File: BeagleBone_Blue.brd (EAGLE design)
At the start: 385 parts, among them J1 HEADER_6, P1 PJ-200A, P10 MOLEX_502570-001, P2 CTI_JTAG,DNI, P3 USB-A_Conn._-_87520-xx1xx, P4 mini_USB-B, P5 WE_7499010211A, P6 10118241-001RLF, P8 FEMALE_HEADER_2x23, P9 FEMALE_HEADER_2x23, Q1 DMC56404, Q2 DMC56404, U10 TPD4S012, U11 TDA19988, U12 MT41K256M16HA_-125:E, U13 eMMC,_2GB, U14 LAN8710A, U15 SN74LVC2G241, U2 TPS65217C, U3 SN74LVC1G06DCK, U4 TL5209, U5 IC_AM335X_ZCE_1, U6 SN74LVC1G74DCTR, U7 24LC32A, U8 TPS2051__DGN_, U9 TPD4S012, Y1 32.768kHz, Y2 24MHz, Y3 25.000MHz, Y4 24.576MHz

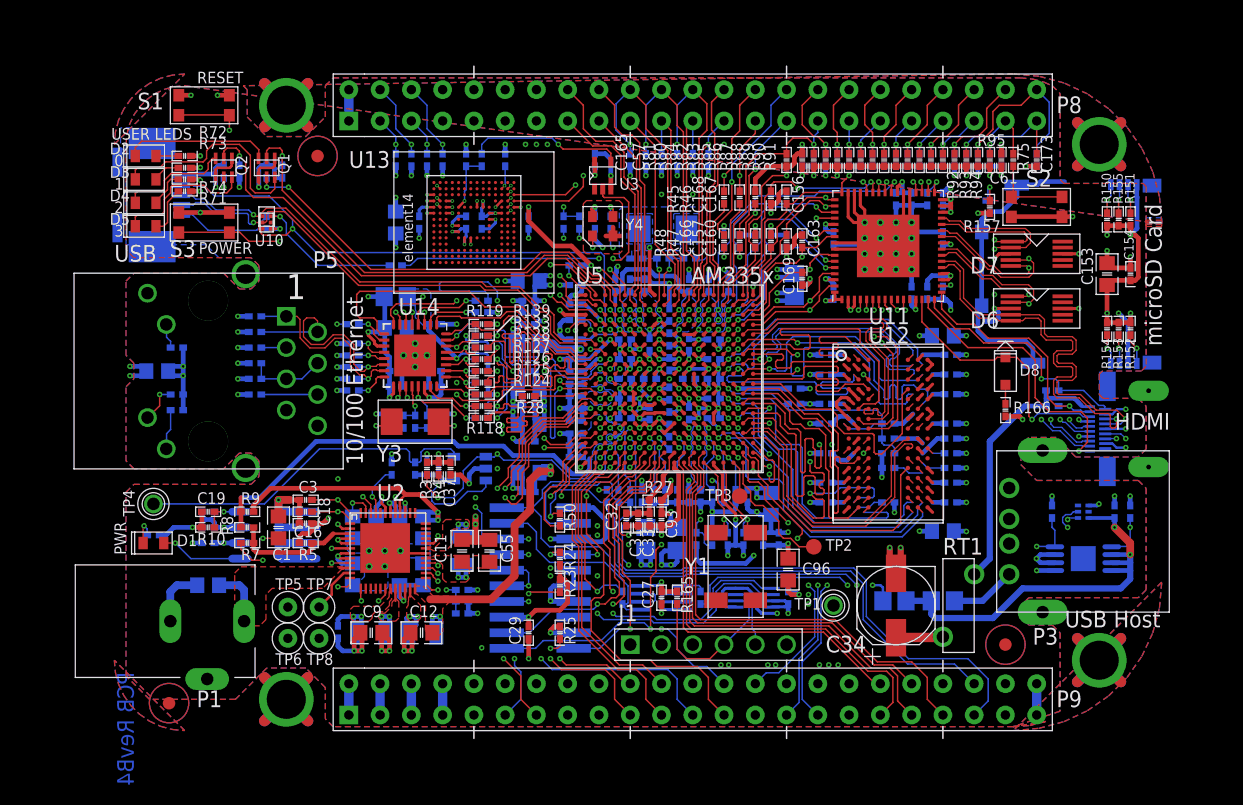
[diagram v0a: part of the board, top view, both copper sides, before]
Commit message: Removed some unused components
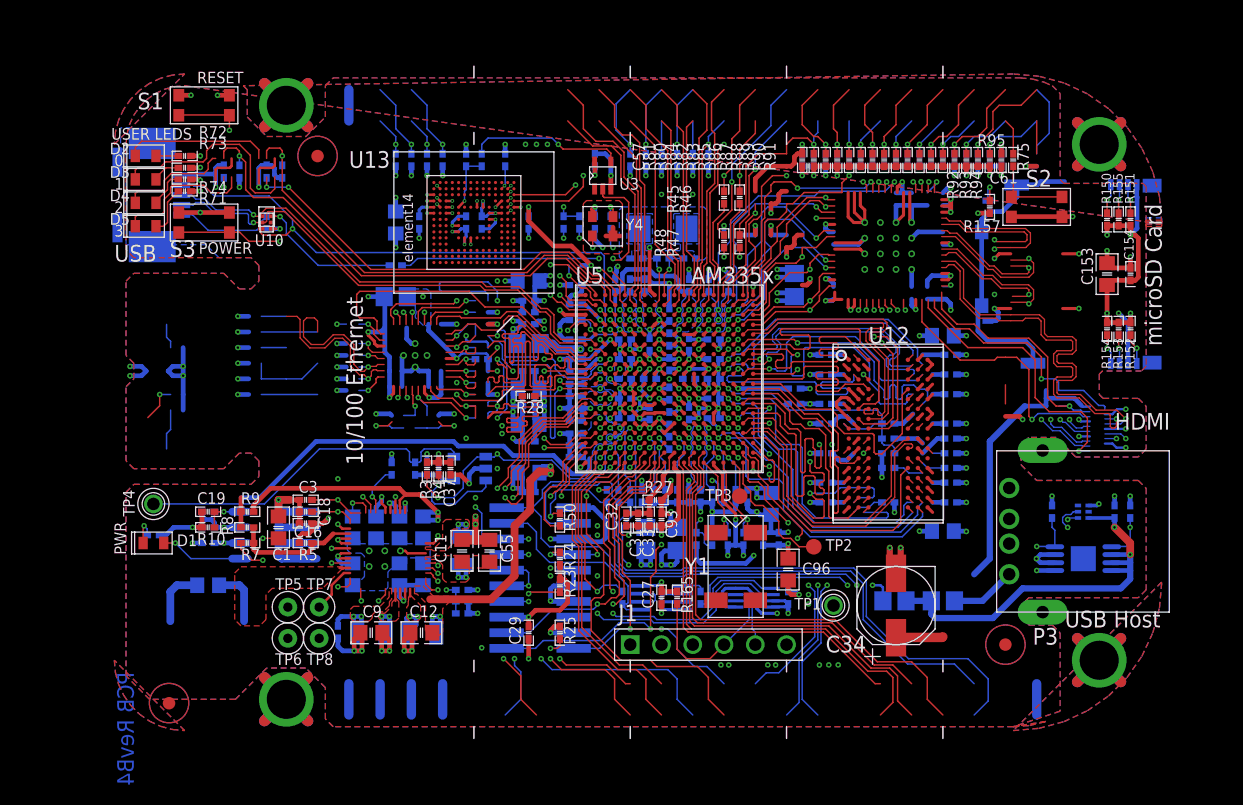
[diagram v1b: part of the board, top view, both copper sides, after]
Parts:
- removed C131, C132, C135, C147, C149, C150: 0.1uf,_6V3, BeagleBone_Black_RevB4:402_1PRIMARY
- removed C133: 10uF,_10V, BeagleBone_Black_RevB4:805_2PRIMARY
- removed C134: 1uF,_10V, BeagleBone_Black_RevB4:402_1PRIMARY
- removed C136: 470pF,_50V, BeagleBone_Black_RevB4:402_2PRIMARY
- removed C137, C138, C139, C140: 15pF,_DNI, BeagleBone_Black_RevB4:402_1PRIMARY
- removed C141: 0.022uF,10V, BeagleBone_Black_RevB4:402_1PRIMARY
- removed C142, C143: 30pF,_50V, BeagleBone_Black_RevB4:402_1PRIMARY
- removed C144, C146, C148, C151: 2.2uF,_6V3, BeagleBone_Black_RevB4:402_2PRIMARY
- removed C145: 0.1uf,_6V3, BeagleBone_Black_RevB4:402_2PRIMARY
- removed C156, C157, C160, C163, C165, C166, C167, C168, C169, C171, C173: 47pF,_6.3V, BeagleBone_Black_RevB4:402_2PRIMARY
- removed C161, C162, C164, C170, C172: 47pF,_6.3V, BeagleBone_Black_RevB4:402_1PRIMARY
- removed D6, D7: IP4283CZ10-TT, BeagleBone_Black_RevB4:TSSOP10_1PRIMARY
- removed D8: RB751V40,115, BeagleBone_Black_RevB4:SOD323_1PRIMARY
- removed P1: PJ-200A, BeagleBone_Black_RevB4:CONN3-PWR-PJ102A_1PRIMARY
- removed P5: WE_7499010211A, BeagleBone_Black_RevB4:RJ45-7499010211A_1PRIMARY
- removed P6: 10118241-001RLF, BeagleBone_Black_RevB4:CONN19_HDMI_1PRIMARY
- removed P8, P9: FEMALE_HEADER_2x23, BeagleBone_Black_RevB4:HEADER23X2_1PRIMARY
- removed Q1, Q2: DMC56404, BeagleBone_Black_RevB4:SMINI6-F3-B_1PRIMARY
- removed R113, R114, R146, R147: 1.5K,_1%, BeagleBone_Black_RevB4:402_1PRIMARY
- removed R115, R116, R117, R135, R145, R158: 10k,_1%, BeagleBone_Black_RevB4:402_1PRIMARY
- removed R118, R148: 10k,_1%, BeagleBone_Black_RevB4:402_2PRIMARY
- removed R119: 1.5K,_1%, BeagleBone_Black_RevB4:402_2PRIMARY
- removed R120, R121, R122, R123: 49.9,_1%, BeagleBone_Black_RevB4:402_1PRIMARY
- removed R124: 10,_1%,DNI, BeagleBone_Black_RevB4:402_2PRIMARY
- removed R125, R126, R127, R128, R133, R139: 100,_1%, BeagleBone_Black_RevB4:402_2PRIMARY
- removed R129, R131, R134, R138: 100,_1%, BeagleBone_Black_RevB4:402_1PRIMARY
- removed R130, R132: 470,_5%, BeagleBone_Black_RevB4:402_1PRIMARY
- removed R136: 0.1,_0805, BeagleBone_Black_RevB4:805_2PRIMARY
- removed R137, R142: 0R,_1%, BeagleBone_Black_RevB4:402_1PRIMARY
- removed R140: 0R,_1%,DNI, BeagleBone_Black_RevB4:402_1PRIMARY
- removed R141: 1M,_1%,DNI, BeagleBone_Black_RevB4:402_2PRIMARY
- removed R143: 10,_1%, BeagleBone_Black_RevB4:402_2PRIMARY
- removed R144: 12.1K,_1%, BeagleBone_Black_RevB4:402_1PRIMARY
- removed R149: 0R,_1%, BeagleBone_Black_RevB4:402_2PRIMARY
- removed R166: 27K,_1%, BeagleBone_Black_RevB4:402_2PRIMARY
- removed RT1: PTC_RXEF010, BeagleBone_Black_RevB4:POLYSW200-5638-310_1PRIMARY
- removed U11: TDA19988, BeagleBone_Black_RevB4:QFN64S9X9P5_1PRIMARY
- removed U14: LAN8710A, BeagleBone_Black_RevB4:QFN32_5X5MM_EP3P3MM_1PRIMARY
- removed U2: TPS65217C, BeagleBone_Black_RevB4:U_48_RSL_1PRIMARY
- removed Y3: 25.000MHz, BeagleBone_Black_RevB4:XTAL150SMD_125X196_1PRIMARY
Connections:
- removed net CRS: R139.2, U14.14
- removed net DVI_+5V: P6.19, R146.1, R147.1, RT1.2
- removed net ETH_TXD4: R145.1, U14.18
- removed net GRNA: P5.10, U14.3
- removed net GRN_C: P5.11, R132.2
- removed net HDMI_CEC: D8.1, P6.15, U11.30
- removed net HDMI_CEC_D: D8.2, R166.1
- removed net HDMI_DSCL: P6.17, R146.2, U11.33
- removed net HDMI_DSDA: P6.18, R147.2, U11.32
- removed net HDMI_HPD: P6.1, U11.31
- removed net HDMI_SWING: R148.1, U11.34
- removed net HDMI_TX0+: D6.2, P6.9, U11.40
- removed net HDMI_TX0-: D6.1, P6.11, U11.39
- removed net HDMI_TX1+: D7.5, P6.6, U11.43
- removed net HDMI_TX1-: D7.4, P6.8, U11.42
- removed net HDMI_TX2+: D7.2, P6.3, U11.45
- removed net HDMI_TX2-: D7.1, P6.5, U11.44
- removed net HDMI_TXC+: D6.4, P6.12, U11.38
- removed net HDMI_TXC-: D6.5, P6.14, U11.37
- removed net MODE2: R113.1, R138.2, U14.15
- removed net NETR149_1: R149.1, U11.49
- removed net PHYX: C142.1, R143.2, Y3.2
- removed net PHY_VDDCR: C134.1, C136.1, U14.6
- removed net PHY_XTAL1: C143.1, R141.2, R142.1, Y3.1
- removed net PHY_XTAL2: R141.1, R143.1, U14.4
- removed net RBIAS: R144.1, U14.32
- removed net RCLKIN: R140.2, R142.2, U14.5
- removed net REFCLKO: R118.1, R124.2, R131.2, U14.7
- removed net RXD1_MODE1: R114.1, R127.2, U14.10
- removed net RXD2_RMIISEL: R117.1, R126.2, U14.9
- removed net RXD3_PHYAD2: R116.1, R125.2, U14.8
- removed net RXDV: R129.2, U14.26
- removed net RXER_PHYAD0: R115.1, R133.2, U14.13
- removed net RXN: C138.1, P5.3, R121.1, U14.30
- removed net RXP: C137.1, P5.2, R120.1, U14.31
- removed net TCT_RCT: C141.1, P5.5, P5.6, R137.1
- removed net TXCLK: R134.2, U14.20
- removed net TXN: C140.1, P5.7, R123.1, U14.28
- removed net TXP: C139.1, P5.4, R122.1, U14.29
- removed net YELA: P5.13, R135.1, U14.2
- removed net YEL_C: P5.12, R130.2
- net 12MHZ: no longer U11.27
- net AIN0: no longer P9.39
- net AIN1: no longer P9.40
- net AIN2: no longer P9.37
- net AIN3: no longer P9.38
- net AIN4: no longer P9.33
- net AIN5: no longer P9.36
- net AIN6: no longer P9.35
- net CLKOUT2: no longer P9.41
- net DGND: no longer C131.2, C132.2, C133.1, C134.2, C135.2, C136.2, C137.2, C138.2, C139.2, C140.2, C141.2, C142.2, C143.2, C144.2, C145.2, C146.2, C147.2, C148.2, C149.2, C150.2, C151.2, C156.2, C157.2, C160.2, C161.2, C162.2, C163.2, C164.2, C165.2, C166.2, C167.2, C168.2, C169.2, C170.2, C171.2, C172.2, C173.2, D6.3, D6.8, D7.3, D7.8, P1.2, P5.9, P6.10, P6.13, P6.16, P6.4, P6.7, P8.1, P8.2, P9.1, P9.2, P9.43, P9.44, P9.45, P9.46, Q1.1, Q1.4, Q2.1, Q2.4, R115.2, R116.2, R117.2, R118.2, R130.1, R132.1, R135.2, R136.1, R144.2, R145.2, R148.2, R149.2, U11.16, U11.17, U11.18, U11.19, U11.53, U11.54, U11.61, U11.62, U11.63, U11.65, U11.8, U11.9, U14.33, U2.30, U2.41, U2.49
- net EHRPWM1A: no longer P9.14
- net EHRPWM1B: no longer P9.16
- net EHRPWM2A: no longer P8.19
- net EHRPWM2B: no longer P8.13
- net GNDA_ADC: no longer P9.34
- net GND_EARTH: no longer P5.14, P5.15, P6.20, P6.21, P6.22, P6.23, R136.2
- net GPIO0_26: no longer P8.14
- net GPIO0_27: no longer P8.17
- net GPIO0_7: no longer P9.42
- net GPIO1_12: no longer P8.12
- net GPIO1_13: no longer P8.11
- net GPIO1_14: no longer P8.16
- net GPIO1_15: no longer P8.15
- net GPIO1_16: no longer P9.15
- net GPIO1_17: no longer P9.23
- net GPIO1_28: no longer P9.12
- net GPIO1_29: no longer P8.26
- net GPIO2_1: no longer P8.18
- net GPIO3_19: no longer P9.27
- net GPIO3_21: no longer P9.25
- net HDMI_1V8: no longer C144.1, C145.1, C146.1, C147.1, C148.1, C149.1, C150.1, C151.1, U11.14, U11.29, U11.35, U11.36, U11.41, U11.46, U11.47, U11.48, U11.5, U11.55
- net HDMI_INT: no longer R158.2, U11.50
- net I2C0_SCL: no longer U11.52, U2.28
- net I2C0_SDA: no longer U11.51, U2.27
- net I2C1_SCL: no longer P9.17
- net I2C1_SDA: no longer P9.18
- net I2C2_SCL: no longer P9.19
- net I2C2_SDA: no longer P9.20
- net LCD_DATA0: no longer C173.1, P8.45, U11.15
- net LCD_DATA1: no longer C171.1, P8.46, U11.13
- net LCD_DATA10: no longer C156.1, P8.36, U11.64
- net LCD_DATA11: no longer C168.1, P8.34, U11.60
- net LCD_DATA12: no longer C167.1, P8.35, U11.59
- net LCD_DATA13: no longer C166.1, P8.33, U11.58
- net LCD_DATA14: no longer C165.1, P8.31, U11.57
- net LCD_DATA15: no longer C164.1, P8.32, U11.56
- net LCD_DATA2: no longer C172.1, P8.43, U11.12
- net LCD_DATA3: no longer C170.1, P8.44, U11.11
- net LCD_DATA4: no longer C169.1, P8.41, U11.10
- net LCD_DATA5: no longer C163.1, P8.42, U11.7
- net LCD_DATA6: no longer C162.1, P8.39, U11.6
- net LCD_DATA7: no longer C161.1, P8.40, U11.3
- net LCD_DATA8: no longer C160.1, P8.37, U11.2
- net LCD_DATA9: no longer C157.1, P8.38, U11.1
- net LCD_DE: no longer P8.30, U11.20
- net LCD_HSYNC: no longer P8.29, U11.22
- net LCD_PCLK: no longer P8.28, U11.4
- net LCD_VSYNC: no longer P8.27, U11.21
- net LDO_PGOOD: no longer U2.46
- net LEDAC: no longer Q1.6
- net LEDBC: no longer Q1.3
- net LEDCC: no longer Q2.6
- net LEDDC: no longer Q2.3
- net MDIO_CLK: no longer U14.17
- net MDIO_DATA: no longer R119.2, U14.16
- net MII1_COL: no longer R138.1
- net MII1_CRS_DV: no longer R139.1
- net MII1_REFCLK: no longer R124.1, R140.1
- net MII1_RXCLK: no longer R131.1
- net MII1_RXD0: no longer R128.1
- net MII1_RXD1: no longer R127.1
- net MII1_RXD2: no longer R126.1
- net MII1_RXD3: no longer R125.1
- net MII1_RXDV: no longer R129.1
- net MII1_RXERR: no longer R133.1
- net MII1_TXCLK: no longer R134.1
- net MII1_TXD0: no longer U14.22
- net MII1_TXD1: no longer U14.23
- net MII1_TXD2: no longer U14.24
- net MII1_TXD3: no longer U14.25
- net MII1_TXEN: no longer U14.21
- net MMC1_CLK: no longer P8.21
- net MMC1_CMD: no longer P8.20
- net MMC1_DAT0: no longer P8.25
- net MMC1_DAT1: no longer P8.24
- net MMC1_DAT2: no longer P8.5
- net MMC1_DAT3: no longer P8.6
- net MMC1_DAT4: no longer P8.23
- net MMC1_DAT5: no longer P8.22
- net MMC1_DAT6: no longer P8.3
- net MMC1_DAT7: no longer P8.4
- net NETTP5_1: no longer U2.4, U2.5
- net NETTP6_1: no longer U2.6
- net NETTP7_1: no longer U2.11
- net PMIC_INT: no longer U2.45
- net PMIC_PGOOD: no longer U2.26
- net PMIC_POWR_EN: no longer U2.9
- net PWR_BUT: no longer P9.9, U2.25
- net P_BYPASS: no longer U2.47
- net P_INT_LDO: no longer U2.48
- net P_L1: no longer U2.20
- net P_L2: no longer U2.23
- net P_L3: no longer U2.31
- net RXD0_MODE0: no longer R128.2, U14.11
- net SPI1_CS0: no longer P9.28, U11.25
- net SPI1_D0: no longer P9.29, U11.24
- net SPI1_D1: no longer P9.30
- net SPI1_SCLK: no longer P9.31, U11.23
- net SYS_5V: no longer P9.7, P9.8, RT1.1, U2.2, U2.21, U2.22, U2.32, U2.39, U2.42, U2.7, U2.8
- net SYS_RESETN: no longer P9.10, U14.19
- net TIMER4: no longer P8.7
- net TIMER5: no longer P8.9
- net TIMER6: no longer P8.10
- net TIMER7: no longer P8.8
- net UART1_RXD: no longer P9.26
- net UART1_TXD: no longer P9.24
- net UART2_RXD: no longer P9.22
- net UART2_TXD: no longer P9.21
- net UART4_RXD: no longer P9.11
- net UART4_TXD: no longer P9.13
- net USB_DC: no longer U2.12
- net USR0: no longer Q1.2
- net USR1: no longer Q1.5
- net USR2: no longer Q2.2
- net USR3: no longer Q2.5
- net VDCDC1: no longer U2.19
- net VDD_1V8: no longer U2.40
- net VDD_3V3A: no longer U2.43
- net VDD_3V3AUX: no longer U2.1
- net VDD_3V3B: no longer C135.1, P9.3, P9.4, R113.2, R114.2, R119.1, R158.1, R166.2, U14.12
- net VDD_5V: no longer P1.1, P9.5, P9.6, U2.10
- net VDD_ADC: no longer P9.32
- net VDD_CORE: no longer U2.29
- net VDD_MPU: no longer U2.24
- net VDD_PHYA: no longer C131.1, C132.1, C133.2, R120.2, R121.2, R122.2, R123.2, R137.2, U14.1, U14.27
- net VIO: no longer U2.18
- net VLDO1: no longer U2.3
- net WAKEUP: no longer U2.13

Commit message: Updates based on review
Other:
- board text removed: "element14"
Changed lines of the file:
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@@
 <text x="459.610459375" y="297.233340625" size="1.354659375" layer="21" font="vector" ratio="6" rot="SR90">microSD Card</text>
 <text x="451.736459375" y="274.373340625" size="1.354659375" layer="21" font="vector" ratio="6" rot="SR0">USB Host</text>
-<text x="394.713459375" y="287.581340625" size="1.354659375" layer="21" font="vector" ratio="6" rot="SR90">10/100 Ethernet</text>
 <text x="421.383459375" y="302.313340625" size="1.354659375" layer="21" font="vector" ratio="6" rot="SR0">AM335x</text>
 <text x="374.520459375" y="304.091340625" size="1.354659375" layer="21" font="vector" ratio="6" rot="SR0">USB</text>
-<text x="455.800459375" y="290.438840625" size="1.354659375" layer="21" font="vector" ratio="6" rot="SR0">HDMI</text>
 <text x="381.378459375" y="304.726340625" size="0.948259375" layer="21" font="vector" ratio="5" rot="SR0">POWER</text>
 <wire x1="416.433" y1="316.3062" x2="416.433" y2="317.2714" width="0.127" layer="22"/>
@@
 <text x="339.595459375" y="325.681340625" size="3.386659375" layer="48" font="vector" rot="SR0">R.250 2X</text>
 <text x="850.9" y="45.72" size="2.709340625" layer="48" font="vector" ratio="7">C</text>
-<text x="398.78" y="304.038" size="0.8382" layer="25" font="vector" ratio="14" rot="R90">element14</text>
 </plain>
 <attributes>

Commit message: cleanup all the nonsense import errors from the EAGLE board conversion
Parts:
- removed C5: (no value), frames:DOCFIELD
- removed P10: MOLEX_502570-001, BeagleBone_Black_RevB4:SD-MICRO-SCHA5B0300_1PRIMARY
- removed TP5, TP6, TP7, TP8: TESTPT1, BeagleBone_Black_RevB4:TP60C33D_1PRIMARY
- moved C100 448.2 mm to (57.5, 32.3)
- moved C118 448.2 mm to (76.1, 39.0)
- moved C122 448.2 mm to (76.1, 23.1)
- moved C73 448.2 mm to (57.5, 38.7)
- moved C98 448.2 mm to (57.5, 35.5)
- moved FB7 448.2 mm to (76.1, 17.4)
- moved C1 448.2 mm to (22.1, 23.4)
- moved C10 448.2 mm to (28.1, 19.6)
- moved C102 448.2 mm to (61.5, 22.5)
- moved C103 448.2 mm to (62.7, 22.5)
- moved C104 448.2 mm to (57.3, 26.0)
- moved C105 448.2 mm to (55.4, 26.0)
- moved C106 448.2 mm to (51.8, 43.1)
- moved C107 448.2 mm to (66.5, 37.4)
- moved C108 448.2 mm to (66.5, 35.8)
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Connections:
- removed net NETTP5_1: TP5.1
- removed net NETTP6_1: TP6.1
- removed net NETTP7_1: TP7.1
- new net S$41: MTG1.1
- new net S$42: C36.2, P4.5, R76.2, R77.2, R78.2, R79.2, S1.1, S1.3, S3.1, S3.3, U10.4
- net DGND: no longer C36.2, P10.6, P10.9, P4.5, R76.2, R77.2, R78.2, R79.2, S1.1, S1.3, S3.1, S3.3, TP8.1, U10.4
- net GND_EARTH: no longer MTG1.1, P10.11, P10.12, P10.13, P10.14, P10.15, P10.16
- net MMC0_CD: no longer P10.10
- net MMC0_CLKO: no longer P10.5
- net MMC0_CMD: no longer P10.3
- net MMC0_DAT0: no longer P10.7
- net MMC0_DAT1: no longer P10.8
- net MMC0_DAT2: no longer P10.1
- net MMC0_DAT3: no longer P10.2
- net VDD_3V3B: no longer P10.4
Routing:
- net SYS_5V: track 109.1 -> 15.9 mm, vias 12 -> 2
- net SYS_RESETN: track 91.1 -> 1.90 mm, vias 6 -> 0
- net SPI1_D0: track 81.5 -> 0.00 mm, vias 3 -> 0
- net SPI1_SCLK: track 81.1 -> 0.00 mm, vias 3 -> 0
- net DGND: track 470.3 -> 400.4 mm, vias 189 -> 175
- net GPIO3_21: track 66.1 -> 0.00 mm, vias 3 -> 0
- net PWR_BUT: track 60.6 -> 0.00 mm, vias 2 -> 0
- net GPIO1_17: track 53.5 -> 0.00 mm, vias 2 -> 0
- net GPIO1_16: track 51.3 -> 1.27 mm, vias 1 -> 0
- net LCD_DATA1: track 47.7 -> 0.00 mm, vias 2 -> 0
- net LCD_DATA15: track 46.8 -> 0.00 mm, vias 3 -> 0
- net LCD_DATA3: track 44.9 -> 0.00 mm, vias 3 -> 0
- net CLKOUT2: track 57.6 -> 13.1 mm
- net UART4_TXD: track 44.5 -> 0.00 mm, vias 2 -> 0
- net MMC1_CMD: track 43.6 -> 0.00 mm, vias 2 -> 0
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- removed copper zone on layer 5, net GND_EARTH
- removed copper zone on layer 16, net S$11
- removed copper zone on layer 16, net S$12
- removed copper zone on layer 2, net S$15
- removed copper zone on layer 2, net S$16
- removed copper zone on layer 3, net S$19
- removed copper zone on layer 1, net S$2
- removed copper zone on layer 3, net S$20
- removed copper zone on layer 3, net S$21
- removed copper zone on layer 3, net S$22
- removed copper zone on layer 3, net S$24
- removed copper zone on layer 3, net S$25
- removed copper zone on layer 4, net S$26
- removed copper zone on layer 4, net S$27
- removed copper zone on layer 4, net S$28
- removed copper zone on layer 4, net S$29
- removed copper zone on layer 1, net S$3
- removed copper zone on layer 4, net S$31
- removed copper zone on layer 4, net S$32
- removed copper zone on layer 4, net S$33
- removed copper zone on layer 5, net S$38
- removed copper zone on layer 5, net S$39
- removed copper zone on layer 16, net S$6
- removed copper zone on layer 16, net S$8
- removed copper zone on layer 16, net S$9
- removed copper zone on layer 4, net VDDS
- removed copper zone on layer 4, net VDD_1V8
- removed copper zone on layer 3, net VDD_CORE
- removed copper zone on layer 3, net VDD_MPU
- removed copper zone on layer 4, net VDD_PLL
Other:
- board text removed: ".125"
- board text removed: ".250"
- board text removed: "1.900"
- board text removed: "10/100 Ethernet"
- board text removed: "14"
- board text removed: "16"
- board text removed: "17"
- board text removed: "18"
- board text removed: "19"
- board text removed: "2.025"
- board text removed: "2.150"
- board text removed: "20"
- board text removed: "32"
- board text removed: "33"
- board text removed: "49"
- board text removed: "5"
- board text removed: "64"
- board text removed: "7"
- board text removed: "9"
- board text removed: "A"
- board text removed: "ASSEMBLY COMPONENT SIDE"
- board text removed: "ASSEMBLY SOLDER SIDE"
- board text removed: "BSLK"
- board text removed: "BSLKC"
- board text removed: "C"
- board text removed: "C1"
- board text removed: "C10"
- board text removed: "C100"
- board text removed: "C101"
- board text removed: "C102"
- board text removed: "C103"
- board text removed: "C104"
- board text removed: "C105"
- board text removed: "C106"
- board text removed: "C107"
- board text removed: "C108"
- board text removed: "C109"
- board text removed: "C11"
- board text removed: "C110"
- board text removed: "C111"
- board text removed: "C112"
- board text removed: "C113"
- board text removed: "C114"
- board text removed: "C115"
- board text removed: "C116"
- board text removed: "C117"
- board text removed: "C118"
- board text removed: "C119"
- board text removed: "C12"
- board text removed: "C120"
- board text removed: "C121"
- board text removed: "C122"
- board text removed: "C123"
- board text removed: "C124"
- board text removed: "C125"
- board text removed: "C126"
- board text removed: "C127"
- board text removed: "C128"
- board text removed: "C129"
- board text removed: "C13"
- board text removed: "C130"
- board text removed: "C131"
- board text removed: "C132"
- board text removed: "C133"
- board text removed: "C134"
- board text removed: "C135"
- board text removed: "C136"
- board text removed: "C137"
- board text removed: "C138"
- board text removed: "C139"
- board text removed: "C14"
- board text removed: "C140"
- board text removed: "C141"
- board text removed: "C142"
- board text removed: "C143"
- board text removed: "C144"
- board text removed: "C145"
- board text removed: "C146"
- board text removed: "C147"
- board text removed: "C148"
- board text removed: "C149"
- board text removed: "C15"
- board text removed: "C150"
- board text removed: "C151"
- board text removed: "C152"
- board text removed: "C153"
- board text removed: "C154"
- board text removed: "C155"
- board text removed: "C156"
- board text removed: "C157"
- board text removed: "C158"
- board text removed: "C159"
- board text removed: "C16"
- board text removed: "C160"
- board text removed: "C161"
- board text removed: "C162"
- board text removed: "C163"
- board text removed: "C164"
- board text removed: "C165"
- board text removed: "C166"
- board text removed: "C167"
- board text removed: "C168"
- board text removed: "C169"
- board text removed: "C17"
- board text removed: "C170"
- board text removed: "C171"
- board text removed: "C172"
- board text removed: "C173"
- board text removed: "C18"
- board text removed: "C19"
- board text removed: "C2"
- board text removed: "C20"
- board text removed: "C21"
- board text removed: "C22"
- board text removed: "C24"
- board text removed: "C25"
- board text removed: "C26"
- board text removed: "C27"
- board text removed: "C28"
- board text removed: "C29"
- board text removed: "C3"
- board text removed: "C30"
- board text removed: "C31"
- board text removed: "C32"
- board text removed: "C33"
- board text removed: "C34"
- board text removed: "C35"
- board text removed: "C36"
- board text removed: "C37"
- board text removed: "C38"
- board text removed: "C39"
- board text removed: "C4"
- board text removed: "C40"
- board text removed: "C41"
- board text removed: "C42"
- board text removed: "C43"
- board text removed: "C44"
- board text removed: "C45"
- board text removed: "C46"
- board text removed: "C47"
- board text removed: "C48"
- board text removed: "C49"
- board text removed: "C50"
- board text removed: "C51"
- board text removed: "C52"
- board text removed: "C53"
- board text removed: "C54"
- board text removed: "C55"
- board text removed: "C56"
- board text removed: "C57"
- board text removed: "C58"
- board text removed: "C59"
- board text removed: "C60"
- board text removed: "C61"
- board text removed: "C62"
- board text removed: "C63"
- board text removed: "C64"
- board text removed: "C65"
- board text removed: "C66"
- board text removed: "C67"
- board text removed: "C68"
- board text removed: "C69"
- board text removed: "C7"
- board text removed: "C70"
- board text removed: "C71"
- board text removed: "C72"
- board text removed: "C73"
- board text removed: "C74"
- board text removed: "C75"
- board text removed: "C76"
- board text removed: "C77"
- board text removed: "C78"
- board text removed: "C79"
- board text removed: "C8"
- board text removed: "C80"
- board text removed: "C81"
- board text removed: "C82"
- board text removed: "C83"
- board text removed: "C84"
- board text removed: "C85"
- board text removed: "C86"
- board text removed: "C87"
- board text removed: "C88"
- board text removed: "C89"
- board text removed: "C9"
- board text removed: "C90"
- board text removed: "C91"
- board text removed: "C92"
- board text removed: "C93"
- board text removed: "C94"
- board text removed: "C95"
- board text removed: "C96"
- board text removed: "C97"
- board text removed: "C98"
- board text removed: "C99"
- board text removed: "D1"
- board text removed: "D2"
- board text removed: "D3"
- board text removed: "D4"
- board text removed: "D5"
- board text removed: "D6"
- board text removed: "D7"
- board text removed: "D8"
- board text removed: "E"
- board text removed: "FB1"
- board text removed: "FB2"
- board text removed: "FB3"
- board text removed: "FB4"
- board text removed: "FB5"
- board text removed: "FB7"
- board text removed: "FB8"
- board text removed: "G"
- board text removed: "HDMI"
- board text removed: "J"
- board text removed: "J1"
- board text removed: "L"
- board text removed: "L1"
- board text removed: "L2"
- board text removed: "L3"
- board text removed: "N"
- board text removed: "P"
- board text removed: "P1"
- board text removed: "P10"
- board text removed: "P2"
- board text removed: "P3"
- board text removed: "P4"
- board text removed: "P5"
- board text removed: "P6"
- board text removed: "P8"
- board text removed: "P9"
- board text removed: "PCB RevB4"
- board text removed: "Q1"
- board text removed: "Q2"
- board text removed: "R"
- board text removed: "R.250 2X"
- board text removed: "R.500 2X"
- board text removed: "R1"
- board text removed: "R10"
- board text removed: "R100"
- board text removed: "R101"
- board text removed: "R102"
- board text removed: "R103"
- board text removed: "R104"
- board text removed: "R105"
- board text removed: "R106"
- board text removed: "R107"
- board text removed: "R108"
- board text removed: "R109"
- board text removed: "R11"
- board text removed: "R110"
- board text removed: "R111"
- board text removed: "R112"
- board text removed: "R113"
- board text removed: "R114"
- board text removed: "R115"
- board text removed: "R116"
- board text removed: "R117"
- board text removed: "R118"
- board text removed: "R119"
- board text removed: "R12"
- board text removed: "R120"
- board text removed: "R121"
- board text removed: "R122"
- board text removed: "R123"
- board text removed: "R124"
- board text removed: "R125"
- board text removed: "R126"
- board text removed: "R127"
- board text removed: "R128"
- board text removed: "R129"
- board text removed: "R130"
- board text removed: "R131"
- board text removed: "R132"
- board text removed: "R133"
- board text removed: "R134"
- board text removed: "R135"
- board text removed: "R136"
- board text removed: "R137"
- board text removed: "R138"
- board text removed: "R139"
- board text removed: "R14"
- board text removed: "R140"
- board text removed: "R141"
- board text removed: "R142"
- board text removed: "R143"
- board text removed: "R144"
- board text removed: "R145"
- board text removed: "R146"
- board text removed: "R147"
- board text removed: "R148"
- board text removed: "R149"
- board text removed: "R150"
- board text removed: "R151"
- board text removed: "R152"
- board text removed: "R153"
- board text removed: "R154"
- board text removed: "R155"
- board text removed: "R156"
- board text removed: "R157"
- board text removed: "R158"
- board text removed: "R159"
- board text removed: "R160"
- board text removed: "R161"
- board text removed: "R162"
- board text removed: "R163"
- board text removed: "R164"
- board text removed: "R165"
- board text removed: "R166"
- board text removed: "R167"
- board text removed: "R17"
- board text removed: "R18"
- board text removed: "R19"
- board text removed: "R20"
- board text removed: "R21"
- board text removed: "R22"
- board text removed: "R23"
- board text removed: "R24"
- board text removed: "R25"
- board text removed: "R26"
- board text removed: "R27"
- board text removed: "R28"
- board text removed: "R3"
- board text removed: "R4"
- board text removed: "R45"
- board text removed: "R46"
- board text removed: "R47"
- board text removed: "R48"
- board text removed: "R49"
- board text removed: "R5"
- board text removed: "R50"
- board text removed: "R51"
- board text removed: "R52"
- board text removed: "R53"
- board text removed: "R54"
- board text removed: "R55"
- board text removed: "R56"
- board text removed: "R57"
- board text removed: "R58"
- board text removed: "R59"
- board text removed: "R6"
- board text removed: "R60"
- board text removed: "R61"
- board text removed: "R62"
- board text removed: "R63"
- board text removed: "R64"
- board text removed: "R65"
- board text removed: "R66"
- board text removed: "R67"
- board text removed: "R68"
- board text removed: "R69"
- board text removed: "R7"
- board text removed: "R70"
- board text removed: "R71"
- board text removed: "R72"
- board text removed: "R73"
- board text removed: "R74"
- board text removed: "R75"
- board text removed: "R76"
- board text removed: "R77"
- board text removed: "R78"
- board text removed: "R79"
- board text removed: "R8"
- board text removed: "R80"
- board text removed: "R81"
- board text removed: "R82"
- board text removed: "R83"
- board text removed: "R84"
- board text removed: "R85"
- board text removed: "R86"
- board text removed: "R87"
- board text removed: "R88"
- board text removed: "R89"
- board text removed: "R9"
- board text removed: "R90"
- board text removed: "R91"
- board text removed: "R92"
- board text removed: "R93"
- board text removed: "R94"
- board text removed: "R95"
- board text removed: "R96"
- board text removed: "R97"
- board text removed: "R98"
- board text removed: "R99"
- board text removed: "RT1"
- board text removed: "S1"
- board text removed: "S2"
- board text removed: "S3"
- board text removed: "TP1"
- board text removed: "TP2"
- board text removed: "TP3"
- board text removed: "TP4"
- board text removed: "TP5"
- board text removed: "TP6"
- board text removed: "TP7"
- board text removed: "TP8"
- board text removed: "TSLK"
- board text removed: "TSLKC"
- board text removed: "U10"
- board text removed: "U11"
- board text removed: "U12"
- board text removed: "U13"
- board text removed: "U14"
- board text removed: "U15"
- board text removed: "U2"
- board text removed: "U3"
- board text removed: "U4"
- board text removed: "U5"
- board text removed: "U6"
- board text removed: "U7"
- board text removed: "U8"
- board text removed: "U9"
- board text removed: "USB Host"
- board text removed: "V"
- board text removed: "Y1"
- board text removed: "Y2"
- board text removed: "Y3"
- board text removed: "Y4"
- board text removed: "microSD Card"

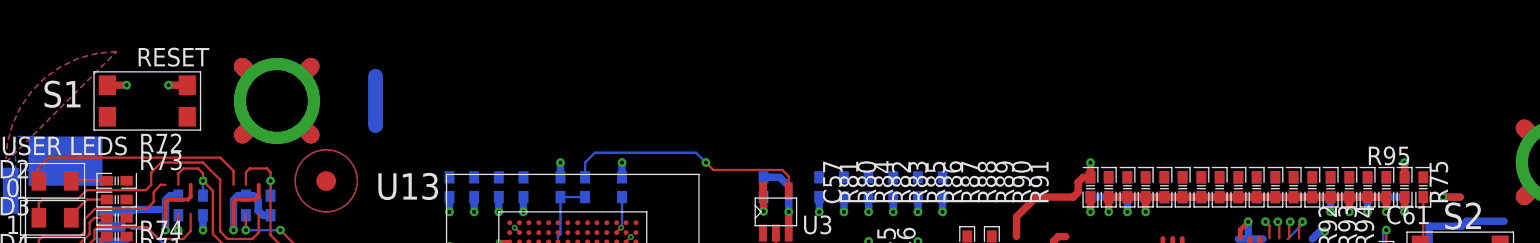
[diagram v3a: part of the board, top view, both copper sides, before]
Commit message: delete old single cell lipo connectors
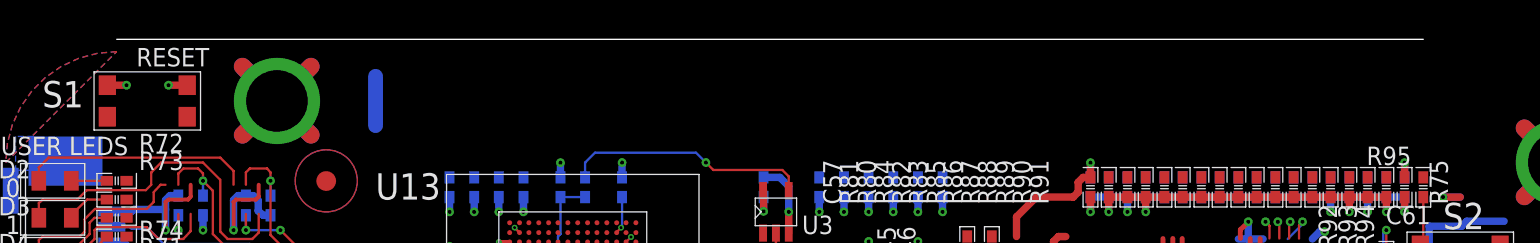
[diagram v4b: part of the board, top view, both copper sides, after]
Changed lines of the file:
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@@
 <wire x1="7.493" y1="6.2738" x2="8.763" y2="6.2738" width="0.0254" layer="48"/>
 <wire x1="8.128" y1="12.6238" x2="8.128" y2="54.5338" width="0.0254" layer="48"/>
-<wire x1="14.478" y1="60.8838" x2="81.788" y2="60.8838" width="0.0254" layer="48"/>
 <wire x1="94.488" y1="18.9738" x2="94.488" y2="48.1838" width="0.0254" layer="48"/>
 <wire x1="14.478" y1="6.2738" x2="81.788" y2="6.2738" width="0.0254" layer="48"/>
@@
 <text x="24.000459375" y="-18.234659375" size="3.386659375" layer="48" font="vector" rot="SR90">.575</text>
 <text x="43.177459375" y="-29.283659375" size="3.386659375" layer="48" font="vector" rot="SR0">3.400</text>
+<wire x1="14.478" y1="60.8838" x2="81.788" y2="60.8838" width="0.0254" layer="20"/>
 </plain>
 <attributes>
